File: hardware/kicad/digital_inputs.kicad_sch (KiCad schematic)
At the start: 10 parts, among them J1201 Logic D0-D7, U1201 SRV05-4, U1202 SRV05-4, U1203 SN74LVC8T245PW

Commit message: feat(hardware)!: draw draft A1 of the schematic around a Pico 2
A Raspberry Pi Pico 2 on two 1x20 sockets replaces the ESP32-S3
development board, the programmable logic device and the buffer
between the two boards (D-39 to D-43 of the specification). The former
interface and range logic sheets become two new ones:

- Controller: the Pico 2, the diodes that join its USB supply and the
  5 V rail of the carrier, resistor arrays in the SPI and acquisition
  lines, a reset button and a console header.
- Side Data: two shift registers that take the range, the status
  signals and the eight logic inputs with every sample.

The DUT connects through a 1x4 pin header and a lever terminal block
in parallel, both GND, VIN, VOUT, GND, and the logic port is a 1x10
header with VCC, GND, D7 to D0: the pin order of the PPK2 (D-44). A
solder jumper selects the supply of the DUT side of the level
translator. A transistor at the driver of the ampere switch holds it
open while VIN is above 5.5 V.

Reference designators are numbered as the annotation tool of KiCad
does by default (D-45). The numbering touches every sheet, so these
changes come in one commit. The symbol and the socket footprint of
the ESP32-S3 board leave the project library; the Pico 2 uses the
symbol and the footprint of the KiCad library.

The electrical rules check reports no errors and no warnings. The
parts stay candidates, and no program for the PIO blocks exists yet.

BREAKING CHANGE: the pins of the controller follow the new pin map of
section 5 of the specification.
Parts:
- added JP2: VOUT / VCC pin, Jumper:SolderJumper-3_P1.3mm_Bridged12_RoundedPad1.0x1.5mm, symbol Jumper:SolderJumper_3_Bridged12
- added R66: 100R, Resistor_SMD:R_0603_1608Metric, symbol Device:R
- J5: renamed from J1201; value Logic D0-D7 -> Logic port; footprint Connector_PinHeader_2.54mm:PinHeader_2x05_P2.54mm_Vertical -> Connector_PinHeader_2.54mm:PinHeader_1x10_P2.54mm_Vertical; Note 2x5 header: pins 1-8 are D0-D7, pins 9-10 ground -> 2.54 mm pin header, straight or angled: VCC, GND, D7 to D0
- renumbered C1201 to C82, C1202 to C83, RN1201 to RN6, RN1202 to RN7, RN1203 to RN8, RN1204 to RN9, U1201 to U27, U1202 to U28, U1203 to U29
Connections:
- net GND: now also J5.2 (Pin_2); no longer J5.10 (Pin_10), J5.9 (Pin_9)
- net VOUT_BUF: now also JP2.1 (A); no longer C82.1, U29.23 (V_{CCB}), U29.24 (V_{CCB})
- net at RN6.1 (R1.1), U27.1 (IO1): now also J5.10 (Pin_10); no longer J5.1 (Pin_1)
- net at RN6.2 (R2.1), U27.3 (IO2): now also J5.9 (Pin_9); no longer J5.2 (Pin_2)
- net at RN6.3 (R3.1), U27.4 (IO3): now also J5.8 (Pin_8); no longer J5.3 (Pin_3)
- net at RN6.4 (R4.1), U27.6 (IO4): now also J5.7 (Pin_7); no longer J5.4 (Pin_4)
- net at RN7.1 (R1.1), U28.1 (IO1): now also J5.6 (Pin_6); no longer J5.5 (Pin_5)
- net at RN7.2 (R2.1), U28.3 (IO2): now also J5.5 (Pin_5); no longer J5.6 (Pin_6)
- net at RN7.3 (R3.1), U28.4 (IO3): now also J5.4 (Pin_4); no longer J5.7 (Pin_7)
- net at RN7.4 (R4.1), U28.6 (IO4): now also J5.3 (Pin_3); no longer J5.8 (Pin_8)
- new net: J5.1 (Pin_1), R66.1
- new net: C82.1, JP2.2 (C), U29.23 (V_{CCB}), U29.24 (V_{CCB})
- new net: JP2.3 (B), R66.2
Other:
- note added: "J5 has the pin order of the PPK2 logic port: pin 1 VCC, pin 2 ground, pins 3 to 10 are logic inputs 7 down to 0. U29 port B is powered through JP2: from VOUT_BUF as built, so the inputs follow the DUT supply, or from the VCC pin of the port for a DUT whose logic runs on another voltage (1.65 V to 5.5 V). DIR and OE are referenced to port A (+3V3_C): DIR low sets the direction B to A. With port B 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"
- note removed: "J1201 is a 2x5 header: pins 1 to 8 are D0 to D7, pins 9 and 10 ground. U1203 port B is powered from VOUT_BUF, so the inputs follow DUT logic levels from 1.65 V to 5.5 V. DIR and OE are referenced to port A (+3V3_C): DIR low sets the direction B to A. With VOUT_BUF off the outputs float; the logic device holds DIN0 to DIN7 with its pull-ups. Each input loads the DUT pin with 1 M to ground."
- title: Digital Inputs D0 to D7 -> Logic Port: Digital Inputs D0 to D7
- moved on the sheet: J5

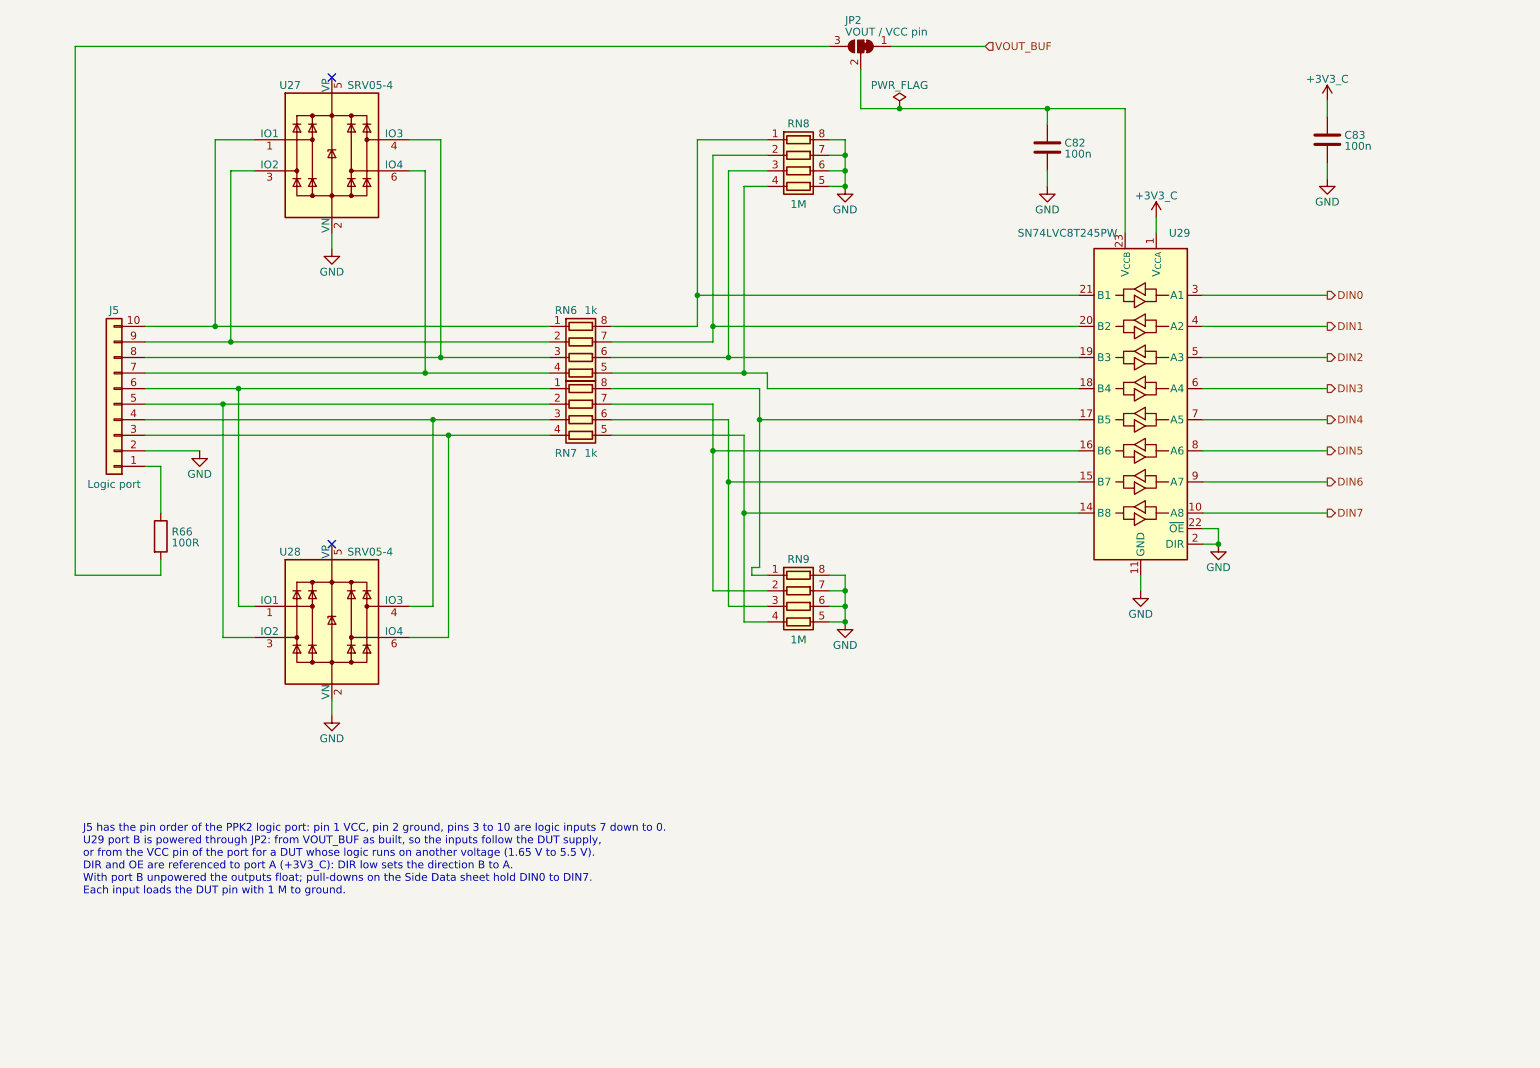
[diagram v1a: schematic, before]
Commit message: feat(hardware): draw draft A2 of the schematic
428 parts on 15 A4 pages, 14 sheets below the root sheet (D-83). Two
sheets are new: Logic Supplies, with the supervisor of the 5 V rail and
the two 3.3 V regulators, and Rail Monitor, with the comparators behind
PWR_GOOD.

The drawings follow the specification of draft A2: a current limiter
on each supply input and a priority multiplexer, a pre-regulator that
tracks the output of the linear regulator, a VIN path that withstands
-20 V to +20 V with its switch open, two diode-connected MOSFETs as
ladder clamp, thin-film and four-terminal shunts, ESD arrays at the CC
pins and at the VCC pin of the logic port. The reference designators
are numbered as KiCad numbers them (D-45), so they are not those of
draft A1.

The project library gains the symbol of the input multiplexer and two
footprints: the lever terminal block with pads of 1.9 mm x 2.3 mm and
the controller module without its antenna keep-out (D-85).

The electrical rules check reports no errors and no warnings. The
parts are candidates, and nothing is built or measured.
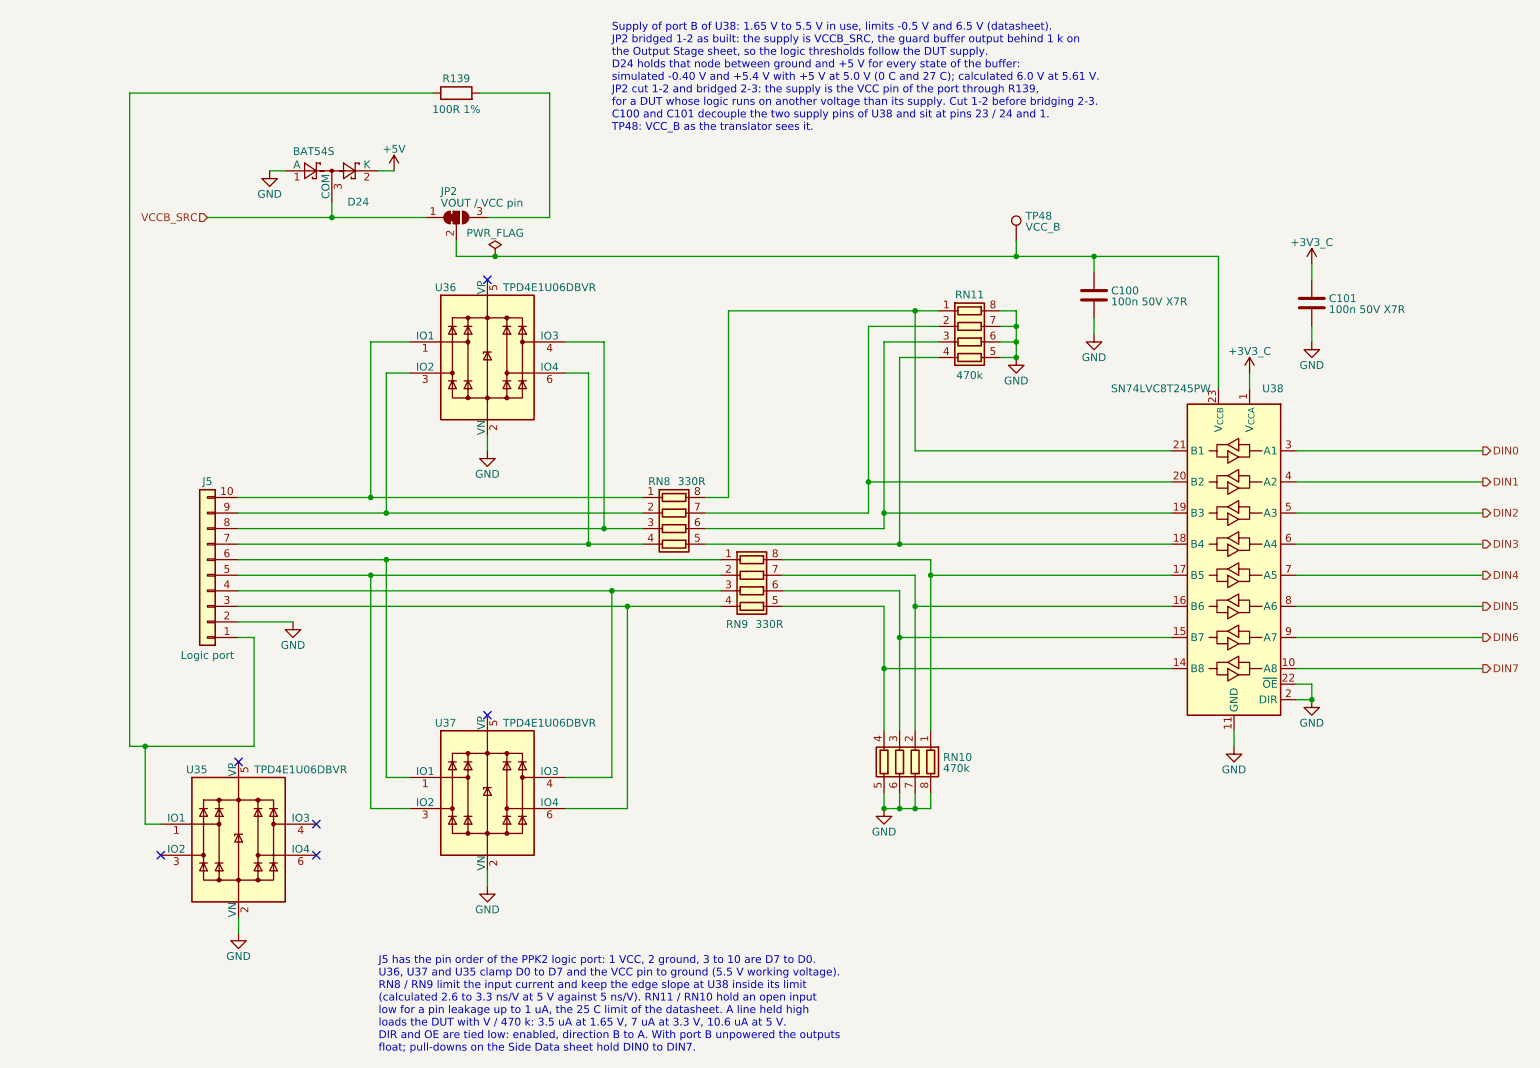
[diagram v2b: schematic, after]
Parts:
- added D24: BAT54S, Package_TO_SOT_SMD:SOT-23, symbol Diode:BAT54S
- added TP48: VCC_B, TestPoint:TestPoint_Pad_D1.5mm, symbol Connector:TestPoint
- added U35: TPD4E1U06DBVR, Package_TO_SOT_SMD:SOT-23-6, symbol Power_Protection:SRV05-4
- C100: renamed from C82; value 100n -> 100n 50V X7R; MPN (none) -> C0603C104K5RACTU; Manufacturer (none) -> KEMET
- C101: renamed from C83; value 100n -> 100n 50V X7R; MPN (none) -> C0603C104K5RACTU; Manufacturer (none) -> KEMET
- J5: MPN (none) -> 61301011121; Manufacturer (none) -> Wurth Elektronik; Note 2.54 mm pin header, straight or angled: VCC, GND, D7 to D0 -> 2.54 mm pin header, straight: VCC, GND, D7 to D0
- JP2: now left out of the parts list
- R139: renamed from R66; value 100R -> 100R 1%; MPN (none) -> CRCW0603100RFKEA; Manufacturer (none) -> Vishay
- RN10: renamed from RN9; value 1M -> 470k; MPN (none) -> CAY16-474J4LF; Manufacturer (none) -> Bourns
- RN11: renamed from RN8; value 1M -> 470k; MPN (none) -> CAY16-474J4LF; Manufacturer (none) -> Bourns
- RN8: renamed from RN6; value 1k -> 330R; MPN (none) -> CAY16-331J4LF; Manufacturer (none) -> Bourns
- RN9: renamed from RN7; value 1k -> 330R; MPN (none) -> CAY16-331J4LF; Manufacturer (none) -> Bourns
- U36: renamed from U27; value SRV05-4 -> TPD4E1U06DBVR; MPN (none) -> TPD4E1U06DBVR; Manufacturer (none) -> Texas Instruments
- U37: renamed from U28; value SRV05-4 -> TPD4E1U06DBVR; MPN (none) -> TPD4E1U06DBVR; Manufacturer (none) -> Texas Instruments
- U38: renamed from U29; MPN (none) -> SN74LVC8T245PWR; Manufacturer (none) -> Texas Instruments
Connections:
- net GND: now also D24.1 (A), U35.2 (VN)
- net at J5.1 (Pin_1), R139.1: now also U35.1 (IO1)
- net at C100.1, JP2.2 (C), U38.23 (V_{CCB})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: now also TP48.1
- net VOUT_BUF renamed VCCB_SRC
- net VCCB_SRC: now also D24.3 (COM)
- new net +5V: D24.2 (K)
- no-connect marks 2 -> 6
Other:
- note added: "J5 has the pin order of the PPK2 logic port: 1 VCC, 2 ground, 3 to 10 are D7 to D0. U36, U37 and U35 clamp D0 to D7 and the VCC pin to ground (5.5 V working voltage). RN8 / RN9 limit the input current and keep the edge slope at U38 inside its limit (calculated 2.6 to 3.3 ns/V at 5 V against 5 ns/V). RN11 / RN10 hold an open input low for a pin leakage up to 1 uA, the 25 C limit of the datasheet. 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"
- note added: "Supply of port B of U38: 1.65 V to 5.5 V in use, limits -0.5 V and 6.5 V (datasheet). JP2 bridged 1-2 as built: the supply is VCCB_SRC, the guard buffer output behind 1 k on the Output Stage sheet, so the logic thresholds follow the DUT supply. D24 holds that node between ground and +5 V for every state of the buffer: simulated -0.40 V and +5.4 V with +5 V at 5.0 V (0 C and 27 C); calculated 6.0 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"
- note removed: "J5 has the pin order of the PPK2 logic port: pin 1 VCC, pin 2 ground, pins 3 to 10 are logic inputs 7 down to 0. U29 port B is powered through JP2: from VOUT_BUF as built, so the inputs follow the DUT supply, or from the VCC pin of the port for a DUT whose logic runs on another voltage (1.65 V to 5.5 V). DIR and OE are referenced to port A (+3V3_C): DIR low sets the direction B to A. With port B 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"
- moved on the sheet: C100, C101, J5, JP2, R139, RN10, RN11, RN8, RN9, U36, U37, U38
